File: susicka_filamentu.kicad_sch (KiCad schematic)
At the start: 35 parts, among them J1 USB_C_Receptacle_USB2.0_16P, J2 Conn_01x03, J3 Conn_01x04, J5 Screw_Terminal_01x02, J6 Conn_01x04, J7 Conn_01x04, Q1 Q_NMOS_GSD, U1 RP2350A-QFN60

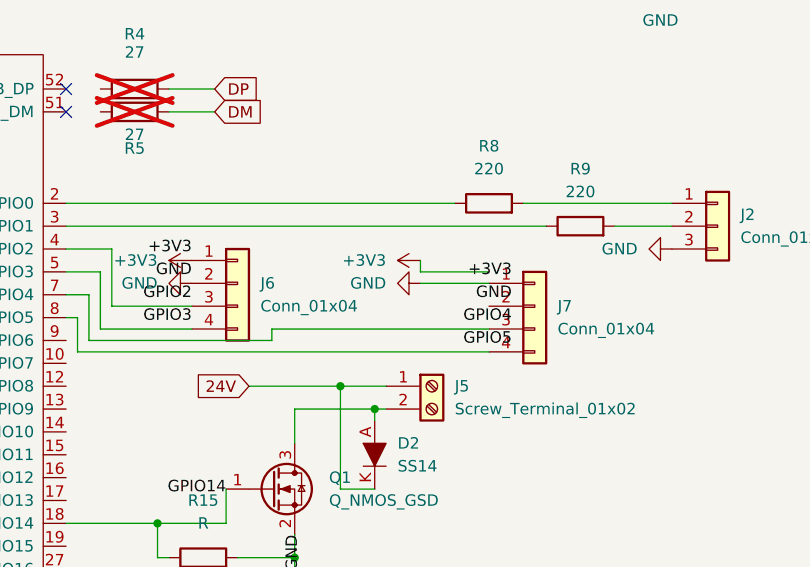
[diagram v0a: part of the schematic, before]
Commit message: Replace Gemini-generated layout with clean project for manual layout
Remove generated scripts, test boards, DRC reports, renders and build
output; restore the sandbox project so the PCB layout can be done by hand.

Co-Authored-By: Claude Opus 5.5 <noreply@anthropic.com>
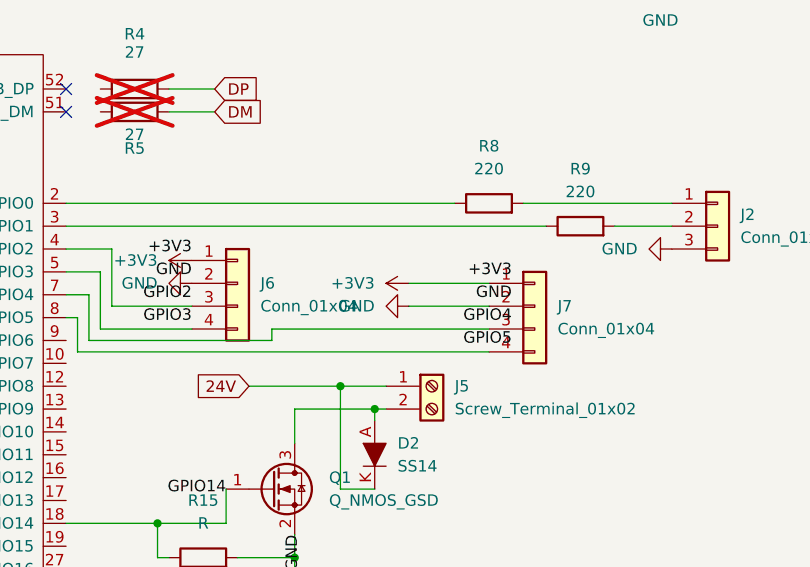
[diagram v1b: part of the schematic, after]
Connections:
- net +3V3: now also J7.1 (Pin_1)
- net GND: now also J7.2 (Pin_2); no longer J7.1 (Pin_1)
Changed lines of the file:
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@@
 	(wire
 		(pts
-			(xy 240.03 71.12) (xy 240.03 69.85)
-		)
-		(stroke
-			(width 0)
-			(type default)
-		)
-	)
-	(wire
-		(pts
 			(xy 21.59 83.82) (xy 30.48 83.82)
 		)
@@
 	(wire
 		(pts
-			(xy 247.65 72.39) (xy 240.03 72.39)
+			(xy 238.76 74.93) (xy 247.65 74.93)
 		)
 		(stroke
@@
 	(wire
 		(pts
-			(xy 247.65 71.12) (xy 240.03 71.12)
-		)
-		(stroke
-			(width 0)
-			(type default)
-		)
-	)
-	(wire
-		(pts
 			(xy 142.24 21.59) (xy 142.24 40.64)
 		)
@@
 	(wire
 		(pts
+			(xy 238.76 72.39) (xy 247.65 72.39)
+		)
+		(stroke
+			(width 0)
+			(type default)
+		)
+	)
+	(wire
+		(pts
 			(xy 220.98 83.82) (xy 231.14 83.82)
 		)
@@
 		)
 	)
+	(label "+3V3"
+		(at 214.63 68.58 180)
+		(effects
+			(font
+				(size 1.27 1.27)
+			)
+			(justify right)
+		)
+	)
+	(label "GND"
+		(at 214.63 71.12 180)
+		(effects
+			(font
+				(size 1.27 1.27)
+			)
+			(justify right)
+		)
+	)
+	(label "GPIO2"
+		(at 214.63 73.66 180)
+		(effects
+			(font
+				(size 1.27 1.27)
+			)
+			(justify right)
+		)
+	)
+	(label "GPIO3"
+		(at 214.63 76.2 180)
+		(effects
+			(font
+				(size 1.27 1.27)
+			)
+			(justify right)
+		)
+	)
+	(label "+3V3"
+		(at 250.19 71.12 180)
+		(effects
+			(font
+				(size 1.27 1.27)
+			)
+			(justify right)
+		)
+	)
+	(label "GND"
+		(at 250.19 73.66 180)
+		(effects
+			(font
+				(size 1.27 1.27)
+			)
+			(justify right)
+		)
+	)
+	(label "GPIO4"
+		(at 250.19 76.2 180)
+		(effects
+			(font
+				(size 1.27 1.27)
+			)
+			(justify right)
+		)
+	)
+	(label "GPIO5"
+		(at 250.19 78.74 180)
+		(effects
+			(font
+				(size 1.27 1.27)
+			)
+			(justify right)
+		)
+	)
+	(label "GPIO14"
+		(at 218.44 95.25 180)
+		(effects
+			(font
+				(size 1.27 1.27)
+			)
+			(justify right)
+		)
+	)
+	(label "GND"
+		(at 226.06 100.33 270)
+		(effects
+			(font
+				(size 1.27 1.27)
+			)
+			(justify right)
+		)
+	)
 	(global_label "DM"
 		(shape input)
@@
 	(symbol
 		(lib_id "power:GND")
-		(at 240.03 72.39 270)
+		(at 238.76 74.93 270)
 		(unit 1)
 		(exclude_from_sim no)
@@
 		(fields_autoplaced yes)
 		(property "Reference" "#PWR045"
-			(at 233.68 72.39 0)
+			(at 232.41 74.93 0)
 			(effects
 				(font
@@
 		)
 		(property "Value" "GND"
-			(at 236.22 72.3899 90)
+			(at 234.95 74.9299 90)
 			(effects
 				(font
@@
 		)
 		(property "Footprint" ""
-			(at 240.03 72.39 0)
+			(at 238.76 74.93 0)
 			(effects
 				(font
@@
 		)
 		(property "Datasheet" ""
-			(at 240.03 72.39 0)
+			(at 238.76 74.93 0)
 			(effects
 				(font
@@
 		)
 		(property "Description" "Power symbol creates a global label with name \"GND\" , ground"
-			(at 240.03 72.39 0)
+			(at 238.76 74.93 0)
 			(effects
 				(font
@@
 	(symbol
 		(lib_id "power:+3V3")
-		(at 240.03 69.85 90)
+		(at 238.76 72.39 90)
 		(unit 1)
 		(exclude_from_sim no)
@@
 		(fields_autoplaced yes)
 		(property "Reference" "#PWR044"
-			(at 243.84 69.85 0)
+			(at 242.57 72.39 0)
 			(effects
 				(font
@@
 		)
 		(property "Value" "+3V3"
-			(at 236.22 69.8499 90)
+			(at 234.95 72.3899 90)
 			(effects
 				(font
@@
 		)
 		(property "Footprint" ""
-			(at 240.03 69.85 0)
+			(at 238.76 72.39 0)
 			(effects
 				(font
@@
 		)
 		(property "Datasheet" ""
-			(at 240.03 69.85 0)
+			(at 238.76 72.39 0)
 			(effects
 				(font
@@
 		)
 		(property "Description" "Power symbol creates a global label with name \"+3V3\""
-			(at 240.03 69.85 0)
+			(at 238.76 72.39 0)
 			(effects
 				(font
@@
 		)
 	)
-	(label "+3V3"
-		(at 214.63 68.58 180)
-		(fields_autoplaced yes)
-		(effects (font (size 1.27 1.27)) (justify right))
-	)
-	(label "GND"
-		(at 214.63 71.12 180)
-		(fields_autoplaced yes)
-		(effects (font (size 1.27 1.27)) (justify right))
-	)
-	(label "GPIO2"
-		(at 214.63 73.66 180)
-		(fields_autoplaced yes)
-		(effects (font (size 1.27 1.27)) (justify right))
-	)
-	(label "GPIO3"
-		(at 214.63 76.20 180)
-		(fields_autoplaced yes)
-		(effects (font (size 1.27 1.27)) (justify right))
-	)
-	(label "+3V3"
-		(at 250.19 71.12 180)
-		(fields_autoplaced yes)
-		(effects (font (size 1.27 1.27)) (justify right))
-	)
-	(label "GND"
-		(at 250.19 73.66 180)
-		(fields_autoplaced yes)
-		(effects (font (size 1.27 1.27)) (justify right))
-	)
-	(label "GPIO4"
-		(at 250.19 76.20 180)
-		(fields_autoplaced yes)
-		(effects (font (size 1.27 1.27)) (justify right))
-	)
-	(label "GPIO5"
-		(at 250.19 78.74 180)
-		(fields_autoplaced yes)
-		(effects (font (size 1.27 1.27)) (justify right))
-	)
-	(label "GPIO14"
-		(at 218.44 95.25 180)
-		(fields_autoplaced yes)
-		(effects (font (size 1.27 1.27)) (justify right))
-	)
-	(label "GND"
-		(at 226.06 100.33 270)
-		(fields_autoplaced yes)
-		(effects (font (size 1.27 1.27)) (justify right))
-	)
-(sheet_instances
+	(sheet_instances
 		(path "/"
 			(page "1")

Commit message: Complete schematic for first prototype
- Footprints: passives 0402/0603 (larger only for 24 V / DC bias),
  U1 and L1 footprints taken from RP2350A Minimal R4 reference (MIT)
- New sheet vystupy: heater (Q1 SiS434DN) with thermal fuse terminal J13,
  fan (GPIO13) and exhaust fan (GPIO12) with AO3422, input protection
  (fuse, AOD4185 reverse polarity, SMBJ24CA TVS, bulk cap), status LED on
  RM2 GPIO0, button GPIO15, NTC on ADC0 (22k pull-up), I2C1 pull-ups,
  second SHT40 on I2C0 (GPIO8/9)
- New sheet rozsireni: spare GPIO header J12, test points TP1-TP5,
  mounting holes H1-H4
- Selected parts with Manufacturer/MPN fields; L2 4.7 uH Wurth 74438356047
- Fix D2 pin mapping (Device:D_Schottky), remove duplicate pull-down R12,
  C16 changed to 100 nF for third DVDD pin, Y1 value set
- Project footprint library susicka.pretty (PowerPAK 1212-8 with G/S/D pads)

Co-Authored-By: Claude Opus 5.5 <noreply@anthropic.com>
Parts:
- removed D2: SS14, Diode_SMD:D_SMA, symbol dk_Diodes-Rectifiers-Single:SS14
- removed J5: Screw_Terminal_01x02, TerminalBlock_Phoenix:TerminalBlock_Phoenix_MKDS-1,5-2_1x02_P5.00mm_Horizontal, symbol Connector:Screw_Terminal_01x02
- removed Q1: Q_NMOS_GSD, Package_TO_SOT_SMD:SOT-23, symbol Transistor_FET:Q_NMOS_GSD
- removed R15: R, Resistor_SMD:R_0603_1608Metric, symbol Device:R
- C10, C11, C12, C13, C14, C15, C17, C7, C8, C9: footprint Capacitor_SMD:C_0603_1608Metric -> Capacitor_SMD:C_0402_1005Metric
- C16: value 4,7 uF -> 100 nF; footprint Capacitor_SMD:C_0603_1608Metric -> Capacitor_SMD:C_0402_1005Metric
- J6: value Conn_01x04 -> SHT4x
- J7: value Conn_01x04 -> HX711
- L1: footprint Inductor_SMD:L_0805_2012Metric -> rp2350A_QFN60:L_Abracon_AOTA-B201610
- U1: footprint rp2350A_QFN60:RP2350A_QFN-60_EP_7.75x7.75_Pitch0.4mm -> rp2350A_QFN60:RP2350A_QFN-60_RPi_Minimal
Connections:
- net SDA0: now reaches U1.12 (GPIO8)
- net SCL0: now reaches U1.13 (GPIO9)
- net GP10: now reaches U1.14 (GPIO10)
- net GP11: now reaches U1.15 (GPIO11)
- net EXH_PWM: now reaches U1.16 (GPIO12)
- net FAN_PWM: now reaches U1.17 (GPIO13)
- net BTN: now reaches U1.19 (GPIO15)
- net GP16: now reaches U1.27 (GPIO16)
- net GP17: now reaches U1.28 (GPIO17)
- net GP18: now reaches U1.29 (GPIO18)
- net GP19: now reaches U1.31 (GPIO19)
- net GP20: now reaches U1.32 (GPIO20)
- net GP21: now reaches U1.33 (GPIO21)
- net GP22: now reaches U1.34 (GPIO22)
- net SDA: now reaches J6.3 (Pin_3), U1.4 (GPIO2)
- net NTC_ADC: now reaches U1.40 (GPIO26_ADC0)
- net GP27: now reaches U1.41 (GPIO27_ADC1)
- net GP28: now reaches U1.42 (GPIO28_ADC2)
- net SCL: now reaches J6.4 (Pin_4), U1.5 (GPIO3)
- net GPIO14 renamed HEAT_PWM
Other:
- added sheet rozsireni (rozsireni.kicad_sch)
- added sheet vystupy (vystupy.kicad_sch)

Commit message: Add communication test points, tidy root sheet, board setup
- Test points TP6-TP19 (1 mm pads) on I2C1, I2C0, HX711, RM2 gSPI,
  heater/fan/exhaust PWM and NTC ADC, plus TP12 GND loop
- Root sheet: GPIO2-5 -> J6/J7 and GPIO24/25/29 -> RM2 now connected by
  global labels (HX711_DT/SCK, WL_DATA/CS/CLK), J6 moved
- Board updated from schematic (F8)
- Board setup: min through-hole 0.2 mm (0.25 mm vias under RP2350),
  new net class Power (1.5 mm track, 0.3 mm clearance, 0.8/0.4 via)
  for 24V_IN, 24V, fuse/heater nets

Co-Authored-By: Claude Opus 5.5 <noreply@anthropic.com>
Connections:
- net HX711_DT: now reaches J7.3 (Pin_3), U1.7 (GPIO4)
- net HX711_SCK: now reaches J7.4 (Pin_4), U1.8 (GPIO5)
- net RM2/RM2_CS renamed WL_CS
- net RM2/RM2_DI renamed WL_DATA
- net RM2/RM2_SCLK renamed WL_CLK
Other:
- moved on the sheet: J6

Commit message: Layout progress, VREG per reference, SI simulation, project notes
- Board: 70x100 mm outline, mounting holes, crystal, RP2350 decoupling,
  VREG copied from RP2350A Minimal R4 (zones, priorities, PGND track),
  RM2 placement and gSPI routing (CLK 16.5 mm, DATA 14.4 mm),
  RF keep-out rule area on all copper layers, test points TP12-TP15
- C4/C5/C6/R7 in 0402; C5/C6 use susicka:C_0402_1005Metric_RPi
  (0.56 mm pad gap so VREG_LX passes under the caps)
- simulace/wl_clk: KiCad ngspice model of WL_CLK (TLINE Z0 ~94 ohm,
  td ~96 ps) for transient and AC (Bode) analysis
- CLAUDE.md and Claude subagents (.claude/agents) moved into the PCB
  branch so the project context is available on other machines
- Ignore KiCad #auto_saved_files#

Co-Authored-By: Claude Opus 5.5 <noreply@anthropic.com>
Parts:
- C4: footprint Capacitor_SMD:C_0603_1608Metric -> Capacitor_SMD:C_0402_1005Metric
- C5, C6: footprint Capacitor_SMD:C_0603_1608Metric -> susicka:C_0402_1005Metric_RPi
- R7: footprint Resistor_SMD:R_0603_1608Metric -> Resistor_SMD:R_0402_1005Metric
